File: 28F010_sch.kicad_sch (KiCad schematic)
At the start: 2 parts

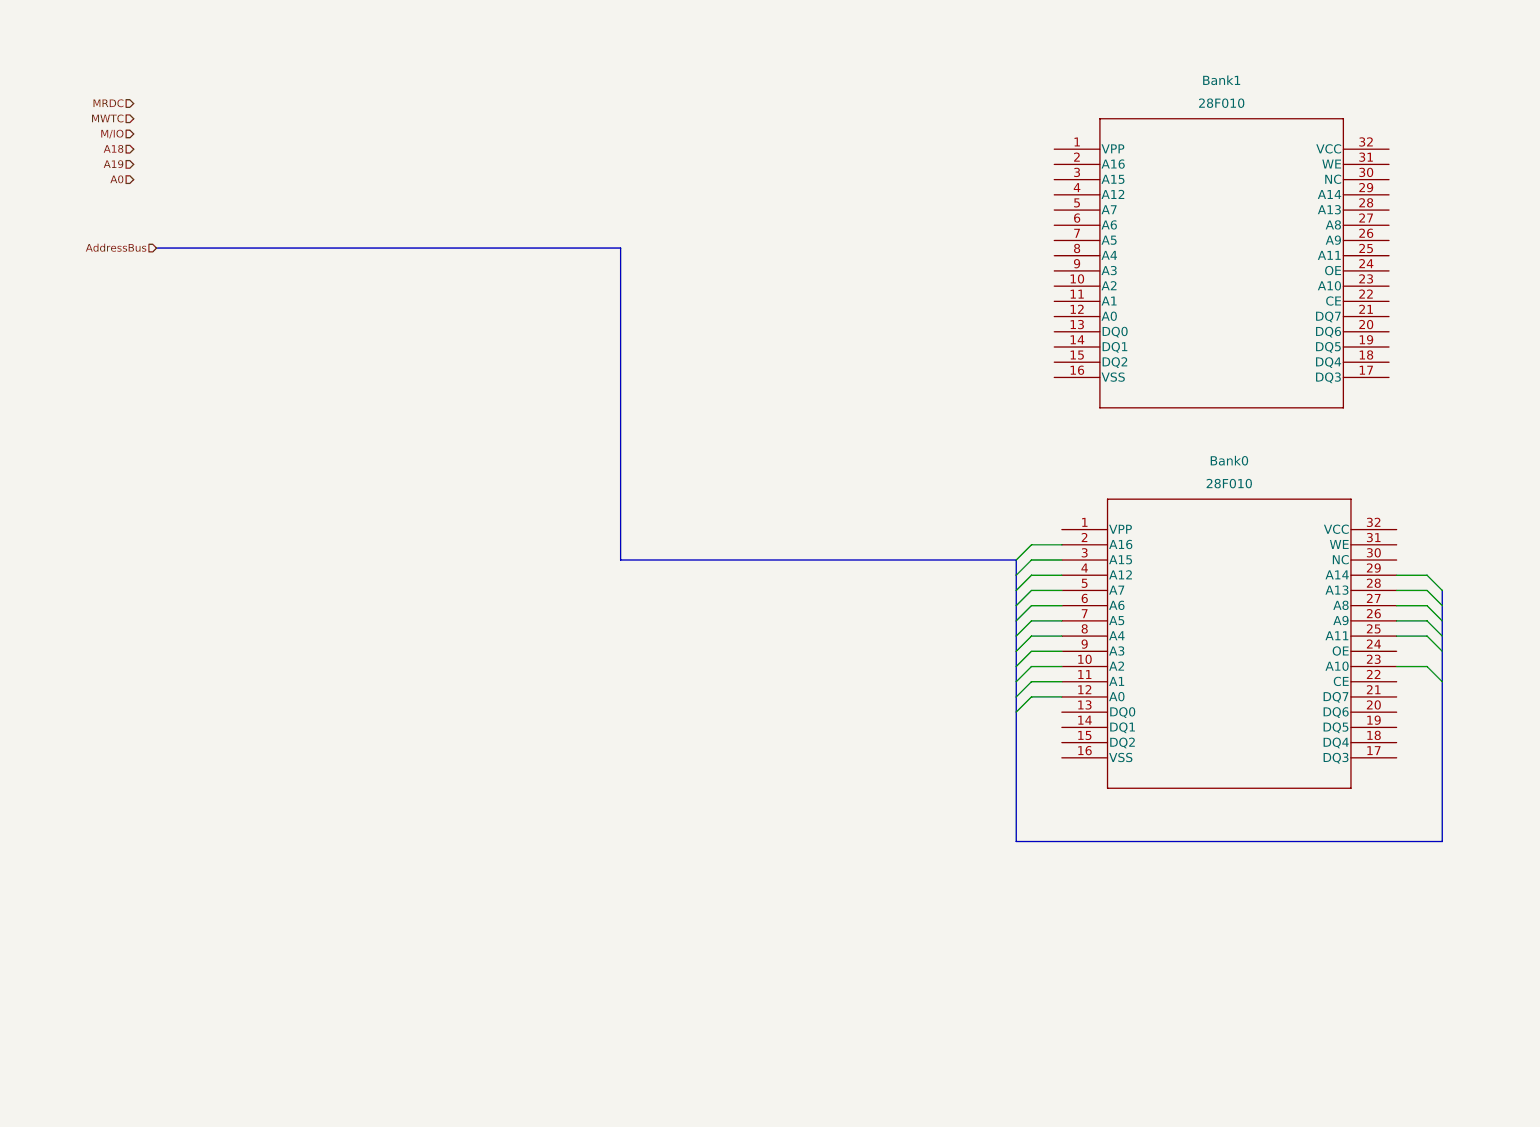
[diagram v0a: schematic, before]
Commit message: More Wiring for the CMOS
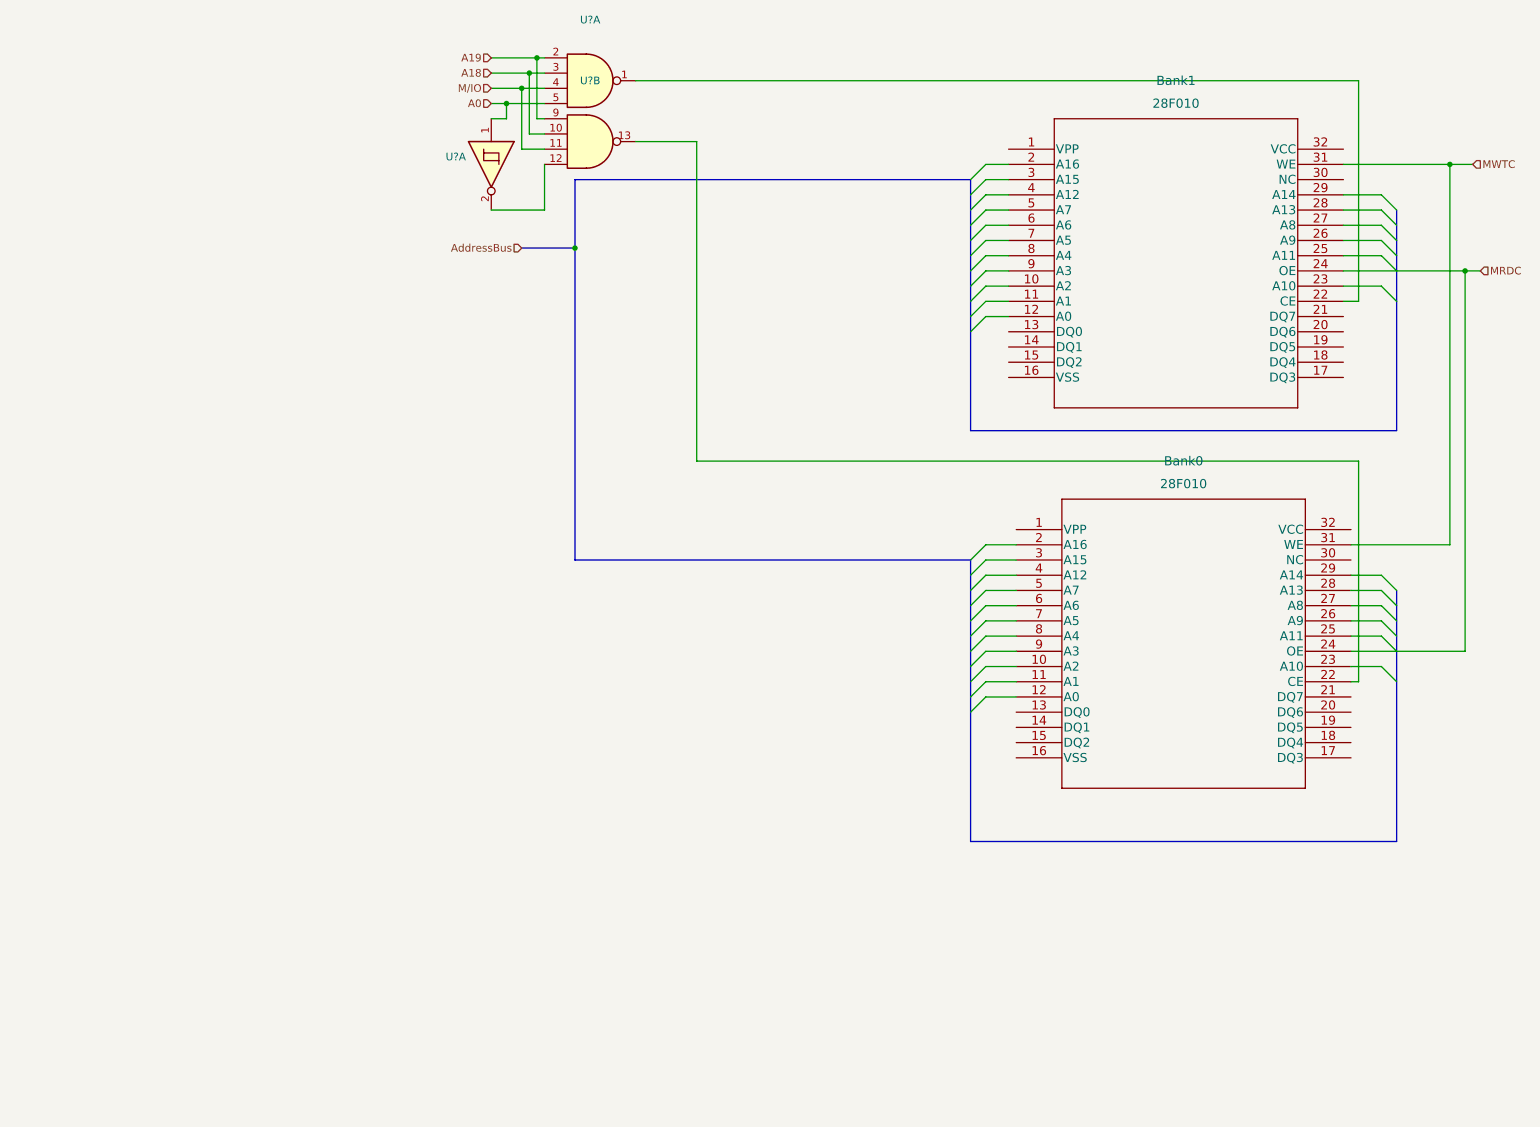
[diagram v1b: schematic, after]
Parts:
- added U? (x2): (no value), symbol 4xxx:4012
- added U?: (no value), symbol 74xx:74LS14
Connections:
- net A0: now also U?.1, U?.5
- net A18: now also U?.10, U?.3
- net A19: now also U?.2, U?.9
- net MRDC: now also Bank0.24 (OE), Bank1.24 (OE)
- net MWTC: now also Bank0.31 (WE), Bank1.31 (WE)
- net M/IO: now also U?.11, U?.4
- net at Bank0.22 (CE): now also U?.13
- net at Bank1.22 (CE): now also U?.1
- new net: U?.12, U?.2
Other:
- moved on the sheet: Bank0, Bank1

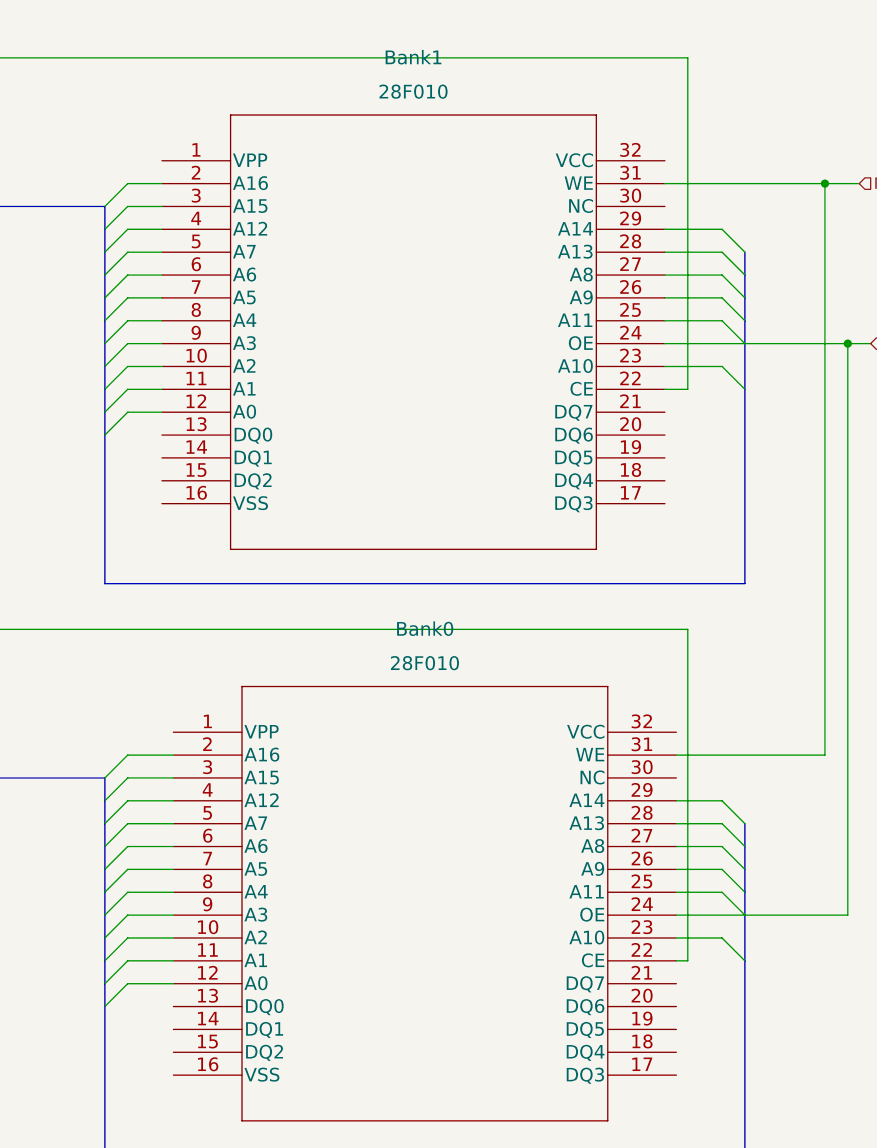
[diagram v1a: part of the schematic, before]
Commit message: Added Labeling for CMOS
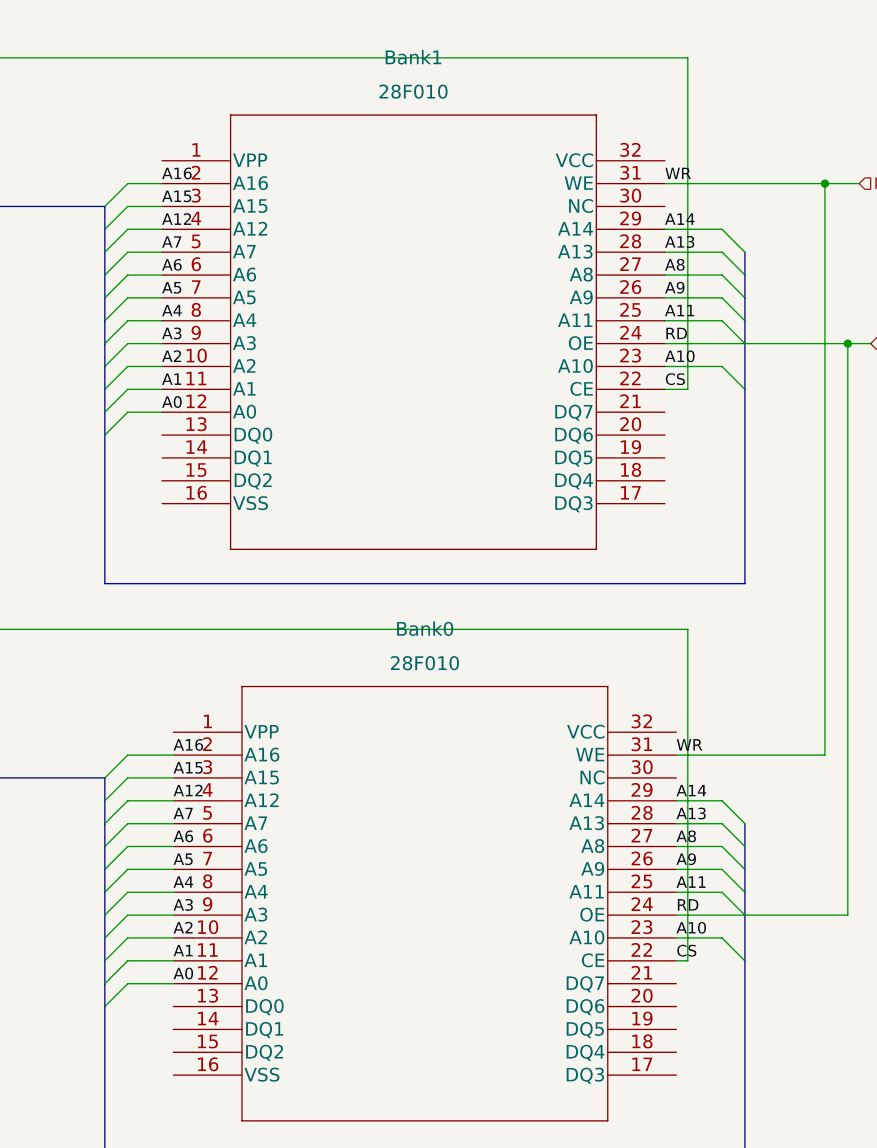
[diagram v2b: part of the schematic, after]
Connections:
- net A0: now also Bank0.12 (A0), Bank1.12 (A0)
- net A2: now reaches Bank0.10 (A2)
- net A2: now also Bank1.10 (A2)
- net A1: now reaches Bank0.11 (A1)
- net A1: now also Bank1.11 (A1)
- net A16: now reaches Bank0.2 (A16)
- net A16: now also Bank1.2 (A16)
- net CS: now reaches Bank0.22 (CE), U?.13
- net CS: now also Bank1.22 (CE), U?.1
- net A10: now reaches Bank0.23 (A10)
- net A10: now also Bank1.23 (A10)
- net A11: now reaches Bank0.25 (A11)
- net A11: now also Bank1.25 (A11)
- net A9: now reaches Bank0.26 (A9)
- net A9: now also Bank1.26 (A9)
- net A8: now reaches Bank0.27 (A8)
- net A8: now also Bank1.27 (A8)
- net A13: now reaches Bank0.28 (A13)
- net A13: now also Bank1.28 (A13)
- net A14: now reaches Bank0.29 (A14)
- net A14: now also Bank1.29 (A14)
- net A15: now reaches Bank0.3 (A15)
- net A15: now also Bank1.3 (A15)
- net A12: now reaches Bank0.4 (A12)
- net A12: now also Bank1.4 (A12)
- net A7: now reaches Bank0.5 (A7)
- net A7: now also Bank1.5 (A7)
- net A6: now reaches Bank0.6 (A6)
- net A6: now also Bank1.6 (A6)
- net A5: now reaches Bank0.7 (A5)
- net A5: now also Bank1.7 (A5)
- net A4: now reaches Bank0.8 (A4)
- net A4: now also Bank1.8 (A4)
- net A3: now reaches Bank0.9 (A3)
- net A3: now also Bank1.9 (A3)
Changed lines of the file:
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@@
     (stroke (width 0) (type default) (color 0 0 0 0))
+  )
+  (label "CS" (at 237.49 55.88 0)
+    (effects (font (size 1.27 1.27)) (justify left bottom))
+  )
+  (label "A5" (at 182.88 109.22 0)
+    (effects (font (size 1.27 1.27)) (justify left bottom))
+  )
+  (label "A8" (at 237.49 43.18 0)
+    (effects (font (size 1.27 1.27)) (justify left bottom))
+  )
+  (label "RD" (at 238.76 114.3 0)
+    (effects (font (size 1.27 1.27)) (justify left bottom))
+  )
+  (label "A7" (at 181.61 40.64 0)
+    (effects (font (size 1.27 1.27)) (justify left bottom))
+  )
+  (label "A5" (at 181.61 45.72 0)
+    (effects (font (size 1.27 1.27)) (justify left bottom))
+  )
+  (label "WR" (at 238.76 96.52 0)
+    (effects (font (size 1.27 1.27)) (justify left bottom))
+  )
+  (label "A7" (at 182.88 104.14 0)
+    (effects (font (size 1.27 1.27)) (justify left bottom))
+  )
+  (label "A14" (at 238.76 101.6 0)
+    (effects (font (size 1.27 1.27)) (justify left bottom))
+  )
+  (label "A11" (at 238.76 111.76 0)
+    (effects (font (size 1.27 1.27)) (justify left bottom))
+  )
+  (label "A4" (at 181.61 48.26 0)
+    (effects (font (size 1.27 1.27)) (justify left bottom))
+  )
+  (label "A1" (at 181.61 55.88 0)
+    (effects (font (size 1.27 1.27)) (justify left bottom))
+  )
+  (label "A15" (at 181.61 35.56 0)
+    (effects (font (size 1.27 1.27)) (justify left bottom))
+  )
+  (label "A3" (at 181.61 50.8 0)
+    (effects (font (size 1.27 1.27)) (justify left bottom))
+  )
+  (label "A0" (at 182.88 121.92 0)
+    (effects (font (size 1.27 1.27)) (justify left bottom))
+  )
+  (label "RD" (at 237.49 50.8 0)
+    (effects (font (size 1.27 1.27)) (justify left bottom))
+  )
+  (label "A12" (at 181.61 38.1 0)
+    (effects (font (size 1.27 1.27)) (justify left bottom))
+  )
+  (label "A3" (at 182.88 114.3 0)
+    (effects (font (size 1.27 1.27)) (justify left bottom))
+  )
+  (label "WR" (at 237.49 33.02 0)
+    (effects (font (size 1.27 1.27)) (justify left bottom))
+  )
+  (label "A16" (at 181.61 33.02 0)
+    (effects (font (size 1.27 1.27)) (justify left bottom))
+  )
+  (label "A0" (at 181.61 58.42 0)
+    (effects (font (size 1.27 1.27)) (justify left bottom))
+  )
+  (label "A9" (at 238.76 109.22 0)
+    (effects (font (size 1.27 1.27)) (justify left bottom))
+  )
+  (label "A4" (at 182.88 111.76 0)
+    (effects (font (size 1.27 1.27)) (justify left bottom))
+  )
+  (label "A1" (at 182.88 119.38 0)
+    (effects (font (size 1.27 1.27)) (justify left bottom))
+  )
+  (label "A15" (at 182.88 99.06 0)
+    (effects (font (size 1.27 1.27)) (justify left bottom))
+  )
+  (label "A13" (at 238.76 104.14 0)
+    (effects (font (size 1.27 1.27)) (justify left bottom))
+  )
+  (label "A2" (at 181.61 53.34 0)
+    (effects (font (size 1.27 1.27)) (justify left bottom))
+  )
+  (label "CS" (at 238.76 119.38 0)
+    (effects (font (size 1.27 1.27)) (justify left bottom))
+  )
+  (label "A12" (at 182.88 101.6 0)
+    (effects (font (size 1.27 1.27)) (justify left bottom))
+  )
+  (label "A8" (at 238.76 106.68 0)
+    (effects (font (size 1.27 1.27)) (justify left bottom))
+  )
+  (label "A2" (at 182.88 116.84 0)
+    (effects (font (size 1.27 1.27)) (justify left bottom))
+  )
+  (label "A9" (at 237.49 45.72 0)
+    (effects (font (size 1.27 1.27)) (justify left bottom))
+  )
+  (label "A6" (at 181.61 43.18 0)
+    (effects (font (size 1.27 1.27)) (justify left bottom))
+  )
+  (label "A6" (at 182.88 106.68 0)
+    (effects (font (size 1.27 1.27)) (justify left bottom))
+  )
+  (label "A16" (at 182.88 96.52 0)
+    (effects (font (size 1.27 1.27)) (justify left bottom))
+  )
+  (label "A13" (at 237.49 40.64 0)
+    (effects (font (size 1.27 1.27)) (justify left bottom))
+  )
+  (label "A10" (at 238.76 116.84 0)
+    (effects (font (size 1.27 1.27)) (justify left bottom))
+  )
+  (label "A14" (at 237.49 38.1 0)
+    (effects (font (size 1.27 1.27)) (justify left bottom))
+  )
+  (label "A11" (at 237.49 48.26 0)
+    (effects (font (size 1.27 1.27)) (justify left bottom))
+  )
+  (label "A10" (at 237.49 53.34 0)
+    (effects (font (size 1.27 1.27)) (justify left bottom))
   )
   (hierarchical_label "A18" (shape input) (at 95.25 17.78 180)
